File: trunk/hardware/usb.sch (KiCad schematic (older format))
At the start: 9 parts, among them J1 USB-MINI-AB, U1 FT232-SSOP28

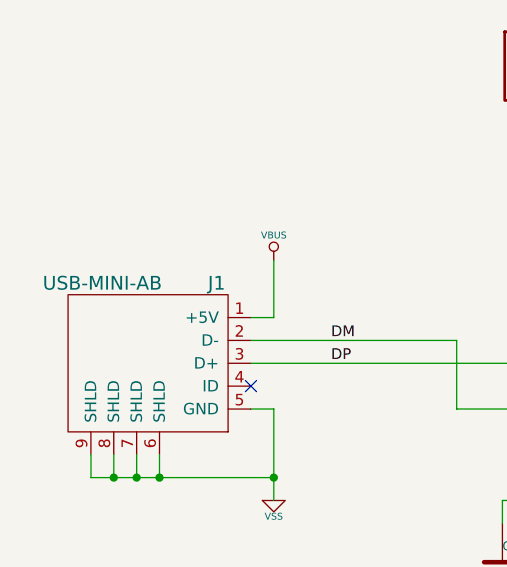
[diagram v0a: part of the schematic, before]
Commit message: Re-worked the RF transmission line circuitry.
I'm frustrated. I've searched high and low for line impedance calculators and I
keep getting the same answers I did the first time around. But my tracks are
much more narrow and more closely spaced than Akiba's -- and my RF section has
massive attenuation. Evidently, his version works well and mine quite simply
does not.  Thus, I've now had no choice but to blindly copy his design, as best
I can and hope for the best. 

This is NOT how I like to do things. I want to understand what I am doing and
why.  So, I will keep trying to find the answers, of course. Meanwhile, I want
this particular project DONE.
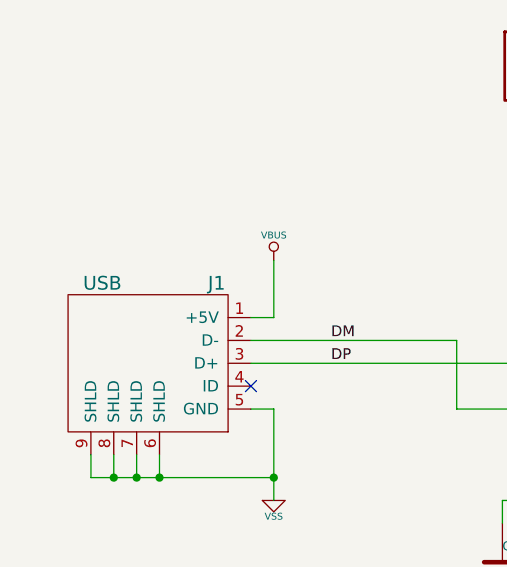
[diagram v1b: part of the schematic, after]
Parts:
- J1: value USB-MINI-AB -> USB
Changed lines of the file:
@@
 Sheet 3 6
 Title "FREAKDUINO-CHIBI 2.4GHz"
-Date "16 aug 2013"
+Date "17 aug 2013"
 Rev "v1.2"
 Comp "KiCAD version by Gruvin"
@@
 P 2800 3500
 F 0 "J1" H 2900 3850 60  0000 C CNN
-F 1 "USB-MINI-AB" H 2400 3850 60  0000 C CNN
+F 1 "USB" H 2400 3850 60  0000 C CNN
 F 2 "" H 2800 3500 60  0000 C CNN
 F 3 "" H 2800 3500 60  0000 C CNN
@@
 $EndComp
 $Comp
-L VSS #PWR028
+L VSS #PWR027
 U 1 1 51E3CBB5
 P 3150 4100
-F 0 "#PWR028" H 3150 4100 30  0001 C CNN
+F 0 "#PWR027" H 3150 4100 30  0001 C CNN
 F 1 "VSS" H 3150 4030 30  0000 C CNN
 F 2 "" H 3150 4100 60  0000 C CNN
@@
 	3150 3300 3150 3050
 $Comp
-L VBUS #PWR029
+L VBUS #PWR028
 U 1 1 51E3CC12
 P 3150 3050
-F 0 "#PWR029" H 3150 3190 20  0001 C CNN
+F 0 "#PWR028" H 3150 3190 20  0001 C CNN
 F 1 "VBUS" H 3150 3160 30  0000 C CNN
 F 2 "" H 3150 3050 60  0000 C CNN
@@
 DP
 $Comp
-L VSS #PWR030
+L VSS #PWR029
 U 1 1 51E3CC1F
 P 5300 5450
-F 0 "#PWR030" H 5300 5450 30  0001 C CNN
+F 0 "#PWR029" H 5300 5450 30  0001 C CNN
 F 1 "VSS" H 5300 5380 30  0000 C CNN
 F 2 "" H 5300 5450 60  0000 C CNN
@@
 Connection ~ 5500 5300
 $Comp
-L VBUS #PWR031
+L VBUS #PWR030
 U 1 1 51E3CC78
 P 5400 2200
-F 0 "#PWR031" H 5400 2340 20  0001 C CNN
+F 0 "#PWR030" H 5400 2340 20  0001 C CNN
 F 1 "VBUS" H 5400 2310 30  0000 C CNN
 F 2 "" H 5400 2200 60  0000 C CNN
@@
 	4200 1950 4200 1750
 $Comp
-L VBUS #PWR032
+L VBUS #PWR031
 U 1 1 51E3CD0B
 P 4200 1750
-F 0 "#PWR032" H 4200 1890 20  0001 C CNN
+F 0 "#PWR031" H 4200 1890 20  0001 C CNN
 F 1 "VBUS" H 4200 1860 30  0000 C CNN
 F 2 "" H 4200 1750 60  0000 C CNN
@@
 $EndComp
 $Comp
-L VSS #PWR033
+L VSS #PWR032
 U 1 1 51E3CD2F
 P 6200 2300
-F 0 "#PWR033" H 6200 2300 30  0001 C CNN
+F 0 "#PWR032" H 6200 2300 30  0001 C CNN
 F 1 "VSS" H 6200 2230 30  0000 C CNN
 F 2 "" H 6200 2300 60  0000 C CNN
@@
 $EndComp
 $Comp
-L VBUS #PWR034
+L VBUS #PWR033
 U 1 1 51E3CD35
 P 6200 1750
-F 0 "#PWR034" H 6200 1890 20  0001 C CNN
+F 0 "#PWR033" H 6200 1890 20  0001 C CNN
 F 1 "VBUS" H 6200 1860 30  0000 C CNN
 F 2 "" H 6200 1750 60  0000 C CNN
@@
 	8400 4000 8400 3700
 $Comp
-L VBUS #PWR035
+L VBUS #PWR034
 U 1 1 51E3CEEA
 P 7900 2450
-F 0 "#PWR035" H 7900 2590 20  0001 C CNN
+F 0 "#PWR034" H 7900 2590 20  0001 C CNN
 F 1 "VBUS" H 7900 2560 30  0000 C CNN
 F 2 "" H 7900 2450 60  0000 C CNN
@@
 $EndComp
 $Comp
-L VBUS #PWR036
+L VBUS #PWR035
 U 1 1 51E3CEF0
 P 8400 2450
-F 0 "#PWR036" H 8400 2590 20  0001 C CNN
+F 0 "#PWR035" H 8400 2590 20  0001 C CNN
 F 1 "VBUS" H 8400 2560 30  0000 C CNN
 F 2 "" H 8400 2450 60  0000 C CNN
@@
 USB_3V3OUT
 $Comp
-L VSS #PWR037
+L VSS #PWR036
 U 1 1 51E3D7CC
 P 6450 4650
-F 0 "#PWR037" H 6450 4650 30  0001 C CNN
+F 0 "#PWR036" H 6450 4650 30  0001 C CNN
 F 1 "VSS" H 6450 4580 30  0000 C CNN
 F 2 "" H 6450 4650 60  0000 C CNN
@@
 	4150 4100 4150 4200
 $Comp
-L VSS #PWR038
+L VSS #PWR037
 U 1 1 51E3D2B6
 P 4150 4750
-F 0 "#PWR038" H 4150 4750 30  0001 C CNN
+F 0 "#PWR037" H 4150 4750 30  0001 C CNN
 F 1 "VSS" H 4150 4680 30  0000 C CNN
 F 2 "" H 4150 4750 60  0000 C CNN

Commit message: OMG LOL. I have the wrong gender SMA connector -- so my antenna was not connecting!
I made the connecton work, by inserting a piece of wire (gender-bender :-P) and
what do you know? Full signal strength! Good grief. 

  \o/
  Yay

Now everything makes sense! LOL Reverting to the r176 design.

I'll locate the correct SMA jack part and update the BOM later.
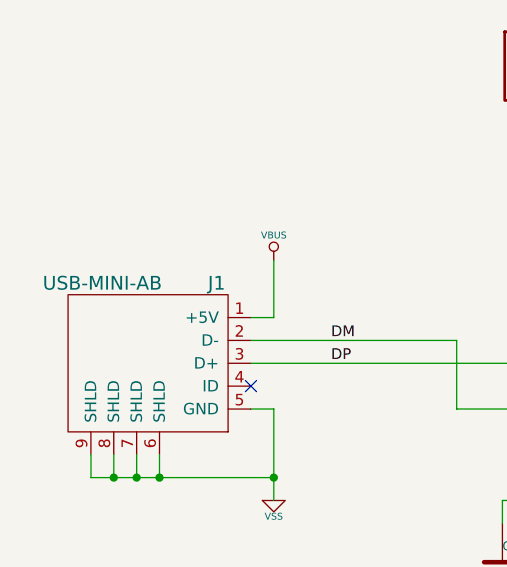
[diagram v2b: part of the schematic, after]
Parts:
- J1: value USB -> USB-MINI-AB
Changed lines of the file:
@@
 Sheet 3 6
 Title "FREAKDUINO-CHIBI 2.4GHz"
-Date "17 aug 2013"
+Date "16 aug 2013"
 Rev "v1.2"
 Comp "KiCAD version by Gruvin"
@@
 P 2800 3500
 F 0 "J1" H 2900 3850 60  0000 C CNN
-F 1 "USB" H 2400 3850 60  0000 C CNN
+F 1 "USB-MINI-AB" H 2400 3850 60  0000 C CNN
 F 2 "" H 2800 3500 60  0000 C CNN
 F 3 "" H 2800 3500 60  0000 C CNN
@@
 $EndComp
 $Comp
-L VSS #PWR027
+L VSS #PWR028
 U 1 1 51E3CBB5
 P 3150 4100
-F 0 "#PWR027" H 3150 4100 30  0001 C CNN
+F 0 "#PWR028" H 3150 4100 30  0001 C CNN
 F 1 "VSS" H 3150 4030 30  0000 C CNN
 F 2 "" H 3150 4100 60  0000 C CNN
@@
 	3150 3300 3150 3050
 $Comp
-L VBUS #PWR028
+L VBUS #PWR029
 U 1 1 51E3CC12
 P 3150 3050
-F 0 "#PWR028" H 3150 3190 20  0001 C CNN
+F 0 "#PWR029" H 3150 3190 20  0001 C CNN
 F 1 "VBUS" H 3150 3160 30  0000 C CNN
 F 2 "" H 3150 3050 60  0000 C CNN
@@
 DP
 $Comp
-L VSS #PWR029
+L VSS #PWR030
 U 1 1 51E3CC1F
 P 5300 5450
-F 0 "#PWR029" H 5300 5450 30  0001 C CNN
+F 0 "#PWR030" H 5300 5450 30  0001 C CNN
 F 1 "VSS" H 5300 5380 30  0000 C CNN
 F 2 "" H 5300 5450 60  0000 C CNN
@@
 Connection ~ 5500 5300
 $Comp
-L VBUS #PWR030
+L VBUS #PWR031
 U 1 1 51E3CC78
 P 5400 2200
-F 0 "#PWR030" H 5400 2340 20  0001 C CNN
+F 0 "#PWR031" H 5400 2340 20  0001 C CNN
 F 1 "VBUS" H 5400 2310 30  0000 C CNN
 F 2 "" H 5400 2200 60  0000 C CNN
@@
 	4200 1950 4200 1750
 $Comp
-L VBUS #PWR031
+L VBUS #PWR032
 U 1 1 51E3CD0B
 P 4200 1750
-F 0 "#PWR031" H 4200 1890 20  0001 C CNN
+F 0 "#PWR032" H 4200 1890 20  0001 C CNN
 F 1 "VBUS" H 4200 1860 30  0000 C CNN
 F 2 "" H 4200 1750 60  0000 C CNN
@@
 $EndComp
 $Comp
-L VSS #PWR032
+L VSS #PWR033
 U 1 1 51E3CD2F
 P 6200 2300
-F 0 "#PWR032" H 6200 2300 30  0001 C CNN
+F 0 "#PWR033" H 6200 2300 30  0001 C CNN
 F 1 "VSS" H 6200 2230 30  0000 C CNN
 F 2 "" H 6200 2300 60  0000 C CNN
@@
 $EndComp
 $Comp
-L VBUS #PWR033
+L VBUS #PWR034
 U 1 1 51E3CD35
 P 6200 1750
-F 0 "#PWR033" H 6200 1890 20  0001 C CNN
+F 0 "#PWR034" H 6200 1890 20  0001 C CNN
 F 1 "VBUS" H 6200 1860 30  0000 C CNN
 F 2 "" H 6200 1750 60  0000 C CNN
@@
 	8400 4000 8400 3700
 $Comp
-L VBUS #PWR034
+L VBUS #PWR035
 U 1 1 51E3CEEA
 P 7900 2450
-F 0 "#PWR034" H 7900 2590 20  0001 C CNN
+F 0 "#PWR035" H 7900 2590 20  0001 C CNN
 F 1 "VBUS" H 7900 2560 30  0000 C CNN
 F 2 "" H 7900 2450 60  0000 C CNN
@@
 $EndComp
 $Comp
-L VBUS #PWR035
+L VBUS #PWR036
 U 1 1 51E3CEF0
 P 8400 2450
-F 0 "#PWR035" H 8400 2590 20  0001 C CNN
+F 0 "#PWR036" H 8400 2590 20  0001 C CNN
 F 1 "VBUS" H 8400 2560 30  0000 C CNN
 F 2 "" H 8400 2450 60  0000 C CNN
@@
 USB_3V3OUT
 $Comp
-L VSS #PWR036
+L VSS #PWR037
 U 1 1 51E3D7CC
 P 6450 4650
-F 0 "#PWR036" H 6450 4650 30  0001 C CNN
+F 0 "#PWR037" H 6450 4650 30  0001 C CNN
 F 1 "VSS" H 6450 4580 30  0000 C CNN
 F 2 "" H 6450 4650 60  0000 C CNN
@@
 	4150 4100 4150 4200
 $Comp
-L VSS #PWR037
+L VSS #PWR038
 U 1 1 51E3D2B6
 P 4150 4750
-F 0 "#PWR037" H 4150 4750 30  0001 C CNN
+F 0 "#PWR038" H 4150 4750 30  0001 C CNN
 F 1 "VSS" H 4150 4680 30  0000 C CNN
 F 2 "" H 4150 4750 60  0000 C CNN
